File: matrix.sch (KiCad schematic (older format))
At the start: 104 parts

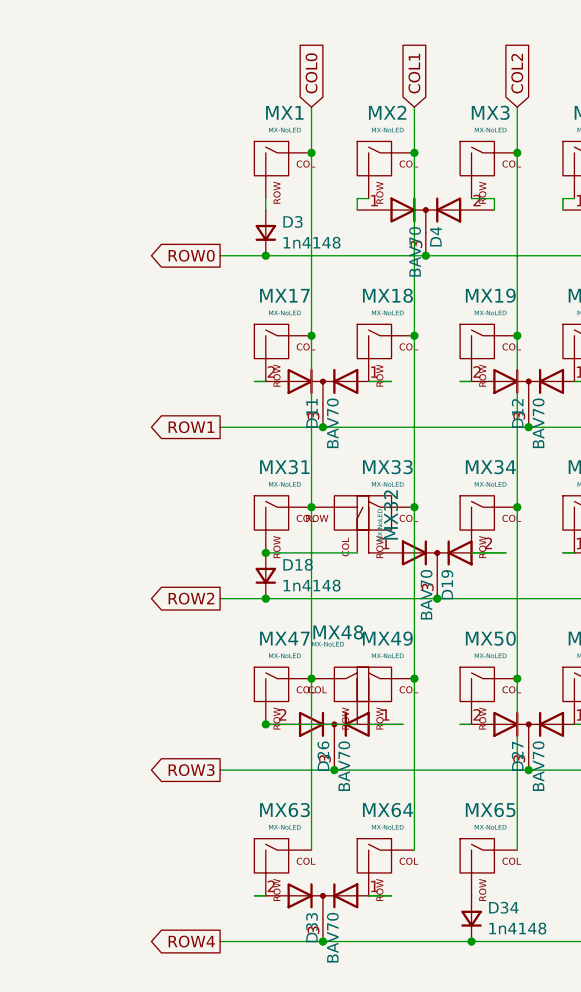
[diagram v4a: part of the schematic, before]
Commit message: added footprint for rotary encoder on esc - renamed v0.4
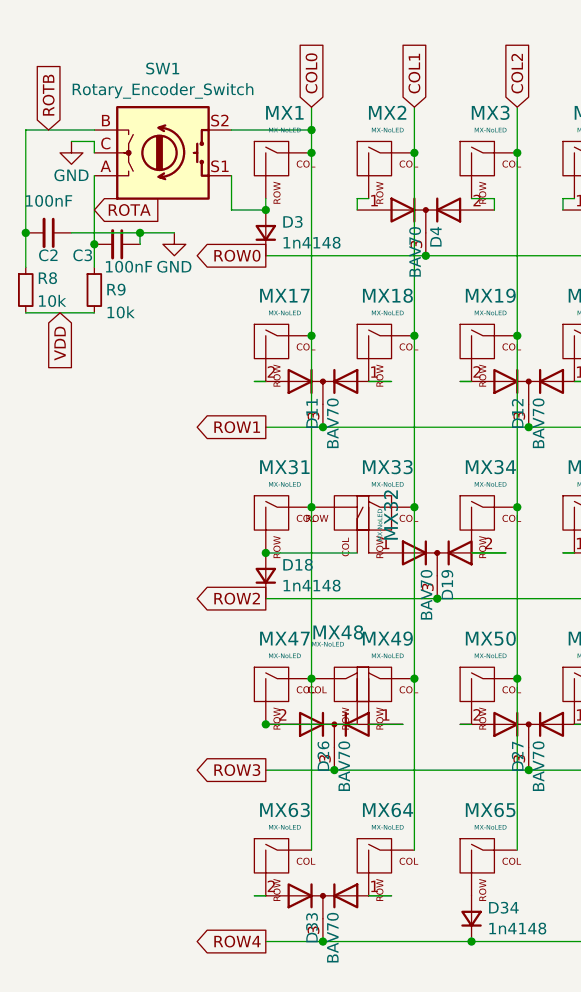
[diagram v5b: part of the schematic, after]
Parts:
- added C2, C3: 100nF, Capacitor_SMD:C_0402_1005Metric, symbol Device:C_Small
- added R8, R9: 10k, Resistor_SMD:R_0603_1608Metric, symbol Device:R_Small
- added SW1: Rotary_Encoder_Switch, Rotary_Encoder:RotaryEncoder_Alps_EC11E-Switch_Vertical_H20mm, symbol Device:Rotary_Encoder_Switch
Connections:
- net COL0: now also SW1.S2
- net at D3.2 (A), MX1.2 (ROW): now also SW1.S1
- new net GND: C2.1, C3.1, SW1.C
- new net ROTA: C3.2, R9.1, SW1.A
- new net ROTB: C2.2, R8.1, SW1.B
- new net VDD: R8.2, R9.2
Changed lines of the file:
@@
 Comment4 ""
 $EndDescr
-Text GLabel 1450 1750 0    50   Output ~ 0
+Text GLabel 1650 1750 0    50   Output ~ 0
 ROW0
 Text GLabel 1850 1100 1    50   Input ~ 0
@@
 	1    0    0    -1
 $EndComp
-Wire Wire Line
-	1850 1100 1850 1300
-Wire Wire Line
-	1450 1750 1650 1750
 $Comp
 L MX_Alps_Hybrid:MX-NoLED MX2
@@
 	1    0    0    -1
 $EndComp
-Text GLabel 1450 2500 0    50   Output ~ 0
+Text GLabel 1650 2500 0    50   Output ~ 0
 ROW1
-Connection ~ 1650 1750
 Text GLabel 2300 1100 1    50   Input ~ 0
 COL1
@@
 	0    -1   -1   0
 $EndComp
-Wire Wire Line
-	1450 3250 1650 3250
 $Comp
 L MX_Alps_Hybrid:MX-NoLED MX47
@@
 	1850 2100 1850 2850
 Connection ~ 1850 2100
-Text GLabel 1450 3250 0    50   Output ~ 0
+Text GLabel 1650 3250 0    50   Output ~ 0
 ROW2
 $Comp
@@
 	8250 2100 8250 3600
 Connection ~ 8250 2100
-Text GLabel 1450 4000 0    50   Output ~ 0
+Text GLabel 1650 4000 0    50   Output ~ 0
 ROW3
-Text GLabel 1450 4750 0    50   Output ~ 0
+Text GLabel 1650 4750 0    50   Output ~ 0
 ROW4
 Connection ~ 8250 3600
@@
 	7950 3050 7550 3050
 Connection ~ 7550 3050
-Connection ~ 1650 3250
 Wire Wire Line
 	7300 3600 7300 4350
@@
 	1    0    0    -1
 $EndComp
-Wire Wire Line
-	1450 2500 1900 2500
 $Comp
 L Diode:BAV70 D11
@@
 	-1   0    0    -1
 $EndComp
-Connection ~ 1900 2500
 Wire Wire Line
 	1600 2300 1650 2300
@@
 Wire Wire Line
 	7100 3050 7200 3050
-Wire Wire Line
-	1450 4000 1950 4000
 $Comp
 L Diode:BAV70 D26
@@
 $EndComp
 Connection ~ 1650 3800
-Connection ~ 1950 4000
 Wire Wire Line
 	2100 3800 2250 3800
@@
 Wire Wire Line
 	8050 3800 8000 3800
-Wire Wire Line
-	1450 4750 1900 4750
-$Comp
-L Diode:BAV70 D33
-U 1 1 60D73C89
-P 1900 4550
-F 0 "D33" V 1946 4480 50  0000 R CNN
-F 1 "BAV70" V 1855 4480 50  0000 R CNN
-F 2 "Package_TO_SOT_SMD:SOT-23" V 1900 4550 50  0001 C CNN
-F 3 "" V 1900 4550 50  0001 C CNN
-F 4 "C68978" H 1900 4550 50  0001 C CNN "JLCPCB"
-	1    1900 4550
-	-1   0    0    -1
-$EndComp
-Connection ~ 1900 4750
-Wire Wire Line
-	1900 4750 2550 4750
 Wire Wire Line
 	1600 4550 1650 4550
@@
 Wire Wire Line
 	8150 1500 8150 1550
+$Comp
+L Device:Rotary_Encoder_Switch SW1
+U 1 1 60C158E2
+P 1200 1300
+F 0 "SW1" H 1200 933 50  0000 C CNN
+F 1 "Rotary_Encoder_Switch" H 1200 1024 50  0000 C CNN
+F 2 "Rotary_Encoder:RotaryEncoder_Alps_EC11E-Switch_Vertical_H20mm" H 1050 1460 50  0001 C CNN
+F 3 "~" H 1200 1560 50  0001 C CNN
+	1    1200 1300
+	1    0    0    1
+$EndComp
+$Comp
+L power:GND #PWR0103
+U 1 1 60C2A547
+P 800 1250
+F 0 "#PWR0103" H 800 1000 50  0001 C CNN
+F 1 "GND" H 800 1100 50  0000 C CNN
+F 2 "" H 800 1250 50  0001 C CNN
+F 3 "" H 800 1250 50  0001 C CNN
+	1    800  1250
+	1    0    0    -1
+$EndComp
+Wire Wire Line
+	900  1300 900  1250
+Wire Wire Line
+	900  1250 800  1250
+Text GLabel 750  2000 3    50   Input ~ 0
+VDD
+$Comp
+L Device:R_Small R9
+U 1 1 60C4BDD1
+P 900 1900
+F 0 "R9" H 950 1900 50  0000 L CNN
+F 1 "10k" H 950 1800 50  0000 L CNN
+F 2 "Resistor_SMD:R_0603_1608Metric" H 900 1900 50  0001 C CNN
+F 3 "~" H 900 1900 50  0001 C CNN
+F 4 "C25804" H 900 1900 50  0001 C CNN "JLCPCB"
+	1    900  1900
+	1    0    0    -1
+$EndComp
+$Comp
+L Device:R_Small R8
+U 1 1 60C4C4DC
+P 600 1900
+F 0 "R8" H 650 1950 50  0000 L CNN
+F 1 "10k" H 650 1850 50  0000 L CNN
+F 2 "Resistor_SMD:R_0603_1608Metric" H 600 1900 50  0001 C CNN
+F 3 "~" H 600 1900 50  0001 C CNN
+F 4 "C25804" H 600 1900 50  0001 C CNN "JLCPCB"
+	1    600  1900
+	1    0    0    -1
+$EndComp
+Text GLabel 700  1200 1    50   Input ~ 0
+ROTB
+Text GLabel 900  1550 2    50   Input ~ 0
+ROTA
+Wire Wire Line
+	600  1200 600  1650
+Wire Wire Line
+	900  1400 900  1700
+$Comp
+L Device:C_Small C2
+U 1 1 60CA635B
+P 700 1650
+F 0 "C2" V 800 1650 50  0000 C CNN
+F 1 "100nF" V 562 1650 50  0000 C CNN
+F 2 "Capacitor_SMD:C_0402_1005Metric" H 700 1650 50  0001 C CNN
+F 3 "~" H 700 1650 50  0001 C CNN
+F 4 "C1525" V 700 1650 50  0001 C CNN "JLCPCB"
+	1    700  1650
+	0    1    1    0
+$EndComp
+Wire Wire Line
+	600  2000 900  2000
+Connection ~ 600  1650
+Wire Wire Line
+	600  1650 600  1800
+Wire Wire Line
+	600  1200 900  1200
+$Comp
+L Device:C_Small C3
+U 1 1 60CC7D82
+P 1000 1700
+F 0 "C3" V 1050 1550 50  0000 C CNN
+F 1 "100nF" V 1100 1750 50  0000 C CNN
+F 2 "Capacitor_SMD:C_0402_1005Metric" H 1000 1700 50  0001 C CNN
+F 3 "~" H 1000 1700 50  0001 C CNN
+F 4 "C1525" V 1000 1700 50  0001 C CNN "JLCPCB"
+	1    1000 1700
+	0    1    1    0
+$EndComp
+Connection ~ 900  1700
+Wire Wire Line
+	900  1700 900  1800
+Wire Wire Line
+	800  1650 1100 1650
+Wire Wire Line
+	1100 1650 1100 1700
+Wire Wire Line
+	1900 2500 1650 2500
+Connection ~ 1900 2500
+Wire Wire Line
+	1950 4000 1650 4000
+Connection ~ 1950 4000
+Wire Wire Line
+	1900 4750 2550 4750
+$Comp
+L Diode:BAV70 D33
+U 1 1 60D73C89
+P 1900 4550
+F 0 "D33" V 1946 4480 50  0000 R CNN
+F 1 "BAV70" V 1855 4480 50  0000 R CNN
+F 2 "Package_TO_SOT_SMD:SOT-23" V 1900 4550 50  0001 C CNN
+F 3 "" V 1900 4550 50  0001 C CNN
+F 4 "C68978" H 1900 4550 50  0001 C CNN "JLCPCB"
+	1    1900 4550
+	-1   0    0    -1
+$EndComp
+Wire Wire Line
+	1900 4750 1650 4750
+Connection ~ 1900 4750
+$Comp
+L power:GND #PWR0104
+U 1 1 60CF581A
+P 1250 1650
+F 0 "#PWR0104" H 1250 1400 50  0001 C CNN
+F 1 "GND" H 1250 1500 50  0000 C CNN
+F 2 "" H 1250 1650 50  0001 C CNN
+F 3 "" H 1250 1650 50  0001 C CNN
+	1    1250 1650
+	1    0    0    -1
+$EndComp
+Wire Wire Line
+	1100 1650 1250 1650
+Connection ~ 1100 1650
+Wire Wire Line
+	1850 1100 1850 1200
+Connection ~ 1850 1200
+Wire Wire Line
+	1850 1200 1850 1300
+Connection ~ 1650 1550
+Wire Wire Line
+	1500 1550 1650 1550
+Wire Wire Line
+	1500 1200 1850 1200
+Wire Wire Line
+	1500 1400 1500 1550
 $EndSCHEMATC

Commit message: updated README
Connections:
- net COL13: no longer MX15.2 (ROW)
- net COL14: now also MX15.2 (ROW)
- net at D10.1 (A), MX14.2 (ROW): no longer MX15.1 (COL)
- net at D10.2 (A), MX16.2 (ROW): now also MX15.1 (COL)
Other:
- moved on the sheet: MX15
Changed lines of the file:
@@
 $EndComp
 Wire Wire Line
-	8250 1100 8250 1300
+	8250 1100 8250 1200
 Text GLabel 8250 1100 1    50   Input ~ 0
 COL14
@@
 Wire Wire Line
 	4400 4750 7100 4750
-$Comp
-L MX_Alps_Hybrid:MX-NoLED MX15
-U 1 1 60F00387
-P 7900 1350
-F 0 "MX15" H 8050 1550 60  0000 R CNN
-F 1 "MX-NoLED" H 8050 1500 20  0000 R CNN
-F 2 "MX_Only:MXOnly-2U-NoLED" H 7275 1325 60  0001 C CNN
-F 3 "" H 7275 1325 60  0001 C CNN
-	1    7900 1350
-	0    1    1    0
-$EndComp
 $Comp
 L MX_Alps_Hybrid:MX-NoLED MX46
@@
 	7200 1500 7200 1550
 Wire Wire Line
-	7950 1500 7550 1500
-Wire Wire Line
 	7550 1500 7550 1550
-Connection ~ 7550 1500
 Wire Wire Line
 	8050 1500 8150 1500
@@
 Wire Wire Line
 	1500 1400 1500 1550
+$Comp
+L MX_Alps_Hybrid:MX-NoLED MX15
+U 1 1 60F00387
+P 7900 1250
+F 0 "MX15" H 8050 1450 60  0000 R CNN
+F 1 "MX-NoLED" H 8050 1400 20  0000 R CNN
+F 2 "MX_Only:MXOnly-2U-NoLED" H 7275 1225 60  0001 C CNN
+F 3 "" H 7275 1225 60  0001 C CNN
+	1    7900 1250
+	0    -1   1    0
+$EndComp
+Wire Wire Line
+	7850 1400 7850 1500
+Wire Wire Line
+	7850 1500 8050 1500
+Connection ~ 8050 1500
+Wire Wire Line
+	8050 1200 8250 1200
+Connection ~ 8250 1200
+Wire Wire Line
+	8250 1200 8250 1300
 $EndSCHEMATC
